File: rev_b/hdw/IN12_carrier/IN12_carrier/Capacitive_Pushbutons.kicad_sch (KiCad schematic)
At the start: 55 parts, among them U905 74LVC1G97, U906 74LVC1G97, U907 74LVC1G97, U908 74LVC1G97, U910 74LVC1G97

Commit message: lots of routing and design progress on IN12 carrier board
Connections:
- net +3V3 renamed +3.3V
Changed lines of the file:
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@@
     )
   )
-  (symbol (lib_id "Analog_Clock-rescue:+3.3V-power") (at 57.15 39.37 0) (unit 1)
+  (symbol (lib_id "power:+3.3V") (at 57.15 39.37 0) (unit 1)
     (in_bom yes) (on_board yes) (dnp no)
     (property "Reference" "#PWR02201" (at 57.15 43.18 0)
@@
     )
   )
-  (symbol (lib_id "Analog_Clock-rescue:+3.3V-power") (at 73.66 140.97 270) (unit 1)
+  (symbol (lib_id "power:+3.3V") (at 73.66 140.97 270) (unit 1)
     (in_bom yes) (on_board yes) (dnp no)
     (property "Reference" "#PWR02209" (at 69.85 140.97 0)
@@
     )
   )
-  (symbol (lib_id "Analog_Clock-rescue:+3.3V-power") (at 57.15 115.57 0) (unit 1)
+  (symbol (lib_id "power:+3.3V") (at 57.15 115.57 0) (unit 1)
     (in_bom yes) (on_board yes) (dnp no)
     (property "Reference" "#PWR02201" (at 57.15 119.38 0)
@@
     )
   )
-  (symbol (lib_id "Analog_Clock-rescue:+3.3V-power") (at 63.5 135.89 0) (unit 1)
+  (symbol (lib_id "power:+3.3V") (at 63.5 135.89 0) (unit 1)
     (in_bom yes) (on_board yes) (dnp no)
     (property "Reference" "#PWR02205" (at 63.5 139.7 0)
@@
     )
   )
-  (symbol (lib_id "Analog_Clock-rescue:+3.3V-power") (at 63.5 97.79 0) (unit 1)
+  (symbol (lib_id "power:+3.3V") (at 63.5 97.79 0) (unit 1)
     (in_bom yes) (on_board yes) (dnp no)
     (property "Reference" "#PWR02205" (at 63.5 101.6 0)
@@
     )
   )
-  (symbol (lib_id "Analog_Clock-rescue:+3.3V-power") (at 63.5 21.59 0) (unit 1)
+  (symbol (lib_id "power:+3.3V") (at 63.5 21.59 0) (unit 1)
     (in_bom yes) (on_board yes) (dnp no)
     (property "Reference" "#PWR02205" (at 63.5 25.4 0)
@@
     )
   )
-  (symbol (lib_id "Analog_Clock-rescue:+3.3V-power") (at 99.06 105.41 0) (unit 1)
+  (symbol (lib_id "power:+3.3V") (at 99.06 105.41 0) (unit 1)
     (in_bom yes) (on_board yes) (dnp no)
     (property "Reference" "#PWR02215" (at 99.06 109.22 0)
@@
     )
   )
-  (symbol (lib_id "Analog_Clock-rescue:+3.3V-power") (at 105.41 39.37 0) (unit 1)
+  (symbol (lib_id "power:+3.3V") (at 105.41 39.37 0) (unit 1)
     (in_bom yes) (on_board yes) (dnp no)
     (property "Reference" "#PWR02219" (at 105.41 43.18 0)
@@
     )
   )
-  (symbol (lib_id "Analog_Clock-rescue:+3.3V-power") (at 73.66 102.87 270) (unit 1)
+  (symbol (lib_id "power:+3.3V") (at 73.66 102.87 270) (unit 1)
     (in_bom yes) (on_board yes) (dnp no)
     (property "Reference" "#PWR02209" (at 69.85 102.87 0)
@@
     )
   )
-  (symbol (lib_id "Analog_Clock-rescue:+3.3V-power") (at 105.41 115.57 0) (unit 1)
+  (symbol (lib_id "power:+3.3V") (at 105.41 115.57 0) (unit 1)
     (in_bom yes) (on_board yes) (dnp no)
     (property "Reference" "#PWR02219" (at 105.41 119.38 0)
@@
     )
   )
-  (symbol (lib_id "Analog_Clock-rescue:+3.3V-power") (at 105.41 77.47 0) (unit 1)
+  (symbol (lib_id "power:+3.3V") (at 105.41 77.47 0) (unit 1)
     (in_bom yes) (on_board yes) (dnp no)
     (property "Reference" "#PWR02219" (at 105.41 81.28 0)
@@
     )
   )
-  (symbol (lib_id "Analog_Clock-rescue:+3.3V-power") (at 63.5 59.69 0) (unit 1)
+  (symbol (lib_id "power:+3.3V") (at 63.5 59.69 0) (unit 1)
     (in_bom yes) (on_board yes) (dnp no)
     (property "Reference" "#PWR02205" (at 63.5 63.5 0)
@@
     )
   )
-  (symbol (lib_id "Analog_Clock-rescue:+3.3V-power") (at 73.66 64.77 270) (unit 1)
+  (symbol (lib_id "power:+3.3V") (at 73.66 64.77 270) (unit 1)
     (in_bom yes) (on_board yes) (dnp no)
     (property "Reference" "#PWR02209" (at 69.85 64.77 0)
@@
     )
   )
-  (symbol (lib_id "Analog_Clock-rescue:+3.3V-power") (at 227.33 29.21 0) (unit 1)
+  (symbol (lib_id "power:+3.3V") (at 227.33 29.21 0) (unit 1)
     (in_bom yes) (on_board yes) (dnp no)
     (property "Reference" "#PWR02215" (at 227.33 33.02 0)
@@
     )
   )
-  (symbol (lib_id "Analog_Clock-rescue:+3.3V-power") (at 99.06 67.31 0) (unit 1)
+  (symbol (lib_id "power:+3.3V") (at 99.06 67.31 0) (unit 1)
     (in_bom yes) (on_board yes) (dnp no)
     (property "Reference" "#PWR02215" (at 99.06 71.12 0)
@@
     )
   )
-  (symbol (lib_id "Analog_Clock-rescue:+3.3V-power") (at 73.66 26.67 270) (unit 1)
+  (symbol (lib_id "power:+3.3V") (at 73.66 26.67 270) (unit 1)
     (in_bom yes) (on_board yes) (dnp no)
     (property "Reference" "#PWR02209" (at 69.85 26.67 0)
@@
     )
   )
-  (symbol (lib_id "Analog_Clock-rescue:+3.3V-power") (at 99.06 143.51 0) (unit 1)
+  (symbol (lib_id "power:+3.3V") (at 99.06 143.51 0) (unit 1)
     (in_bom yes) (on_board yes) (dnp no)
     (property "Reference" "#PWR02215" (at 99.06 147.32 0)
@@
     )
   )
-  (symbol (lib_id "Analog_Clock-rescue:+3.3V-power") (at 57.15 153.67 0) (unit 1)
+  (symbol (lib_id "power:+3.3V") (at 57.15 153.67 0) (unit 1)
     (in_bom yes) (on_board yes) (dnp no)
     (property "Reference" "#PWR02201" (at 57.15 157.48 0)
@@
     )
   )
-  (symbol (lib_id "Analog_Clock-rescue:+3.3V-power") (at 99.06 29.21 0) (unit 1)
+  (symbol (lib_id "power:+3.3V") (at 99.06 29.21 0) (unit 1)
     (in_bom yes) (on_board yes) (dnp no)
     (property "Reference" "#PWR02215" (at 99.06 33.02 0)
@@
     )
   )
-  (symbol (lib_id "Analog_Clock-rescue:+3.3V-power") (at 191.77 21.59 0) (unit 1)
+  (symbol (lib_id "power:+3.3V") (at 191.77 21.59 0) (unit 1)
     (in_bom yes) (on_board yes) (dnp no)
     (property "Reference" "#PWR02205" (at 191.77 25.4 0)
@@
     )
   )
-  (symbol (lib_id "Analog_Clock-rescue:+3.3V-power") (at 233.68 39.37 0) (unit 1)
+  (symbol (lib_id "power:+3.3V") (at 233.68 39.37 0) (unit 1)
     (in_bom yes) (on_board yes) (dnp no)
     (property "Reference" "#PWR02219" (at 233.68 43.18 0)
@@
     )
   )
-  (symbol (lib_id "Analog_Clock-rescue:+3.3V-power") (at 185.42 39.37 0) (unit 1)
+  (symbol (lib_id "power:+3.3V") (at 185.42 39.37 0) (unit 1)
     (in_bom yes) (on_board yes) (dnp no)
     (property "Reference" "#PWR02201" (at 185.42 43.18 0)
@@
     )
   )
-  (symbol (lib_id "Analog_Clock-rescue:+3.3V-power") (at 105.41 153.67 0) (unit 1)
+  (symbol (lib_id "power:+3.3V") (at 105.41 153.67 0) (unit 1)
     (in_bom yes) (on_board yes) (dnp no)
     (property "Reference" "#PWR02219" (at 105.41 157.48 0)
@@
     )
   )
-  (symbol (lib_id "Analog_Clock-rescue:+3.3V-power") (at 201.93 26.67 270) (unit 1)
+  (symbol (lib_id "power:+3.3V") (at 201.93 26.67 270) (unit 1)
     (in_bom yes) (on_board yes) (dnp no)
     (property "Reference" "#PWR02209" (at 198.12 26.67 0)
@@
     )
   )
-  (symbol (lib_id "Analog_Clock-rescue:+3.3V-power") (at 57.15 77.47 0) (unit 1)
+  (symbol (lib_id "power:+3.3V") (at 57.15 77.47 0) (unit 1)
     (in_bom yes) (on_board yes) (dnp no)
     (property "Reference" "#PWR02201" (at 57.15 81.28 0)

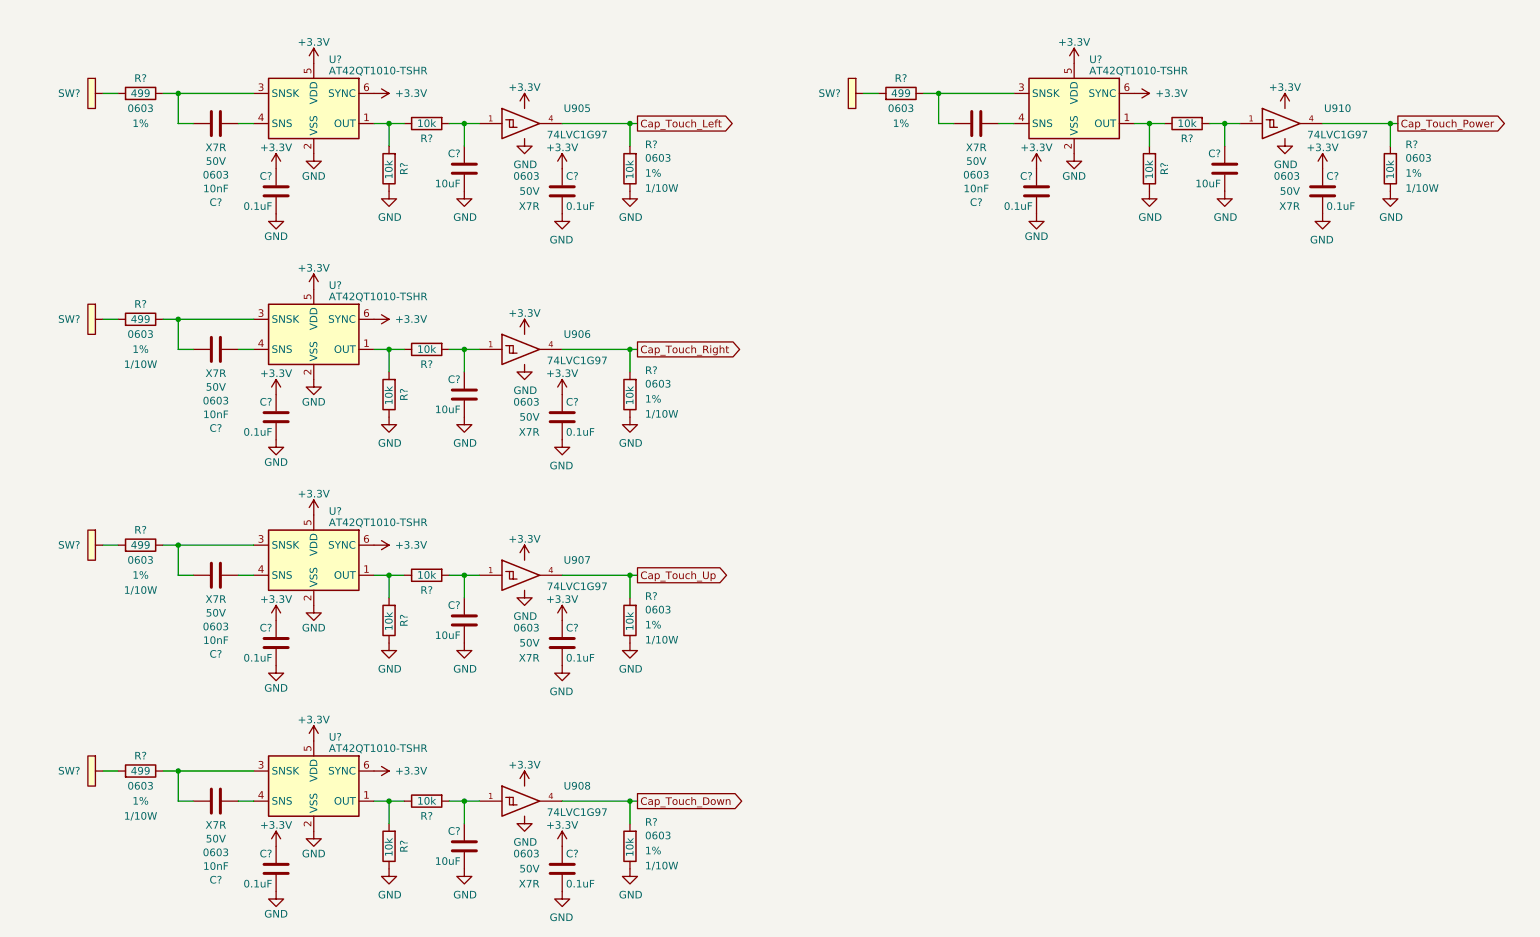
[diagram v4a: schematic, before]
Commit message: added cap touch sensors back
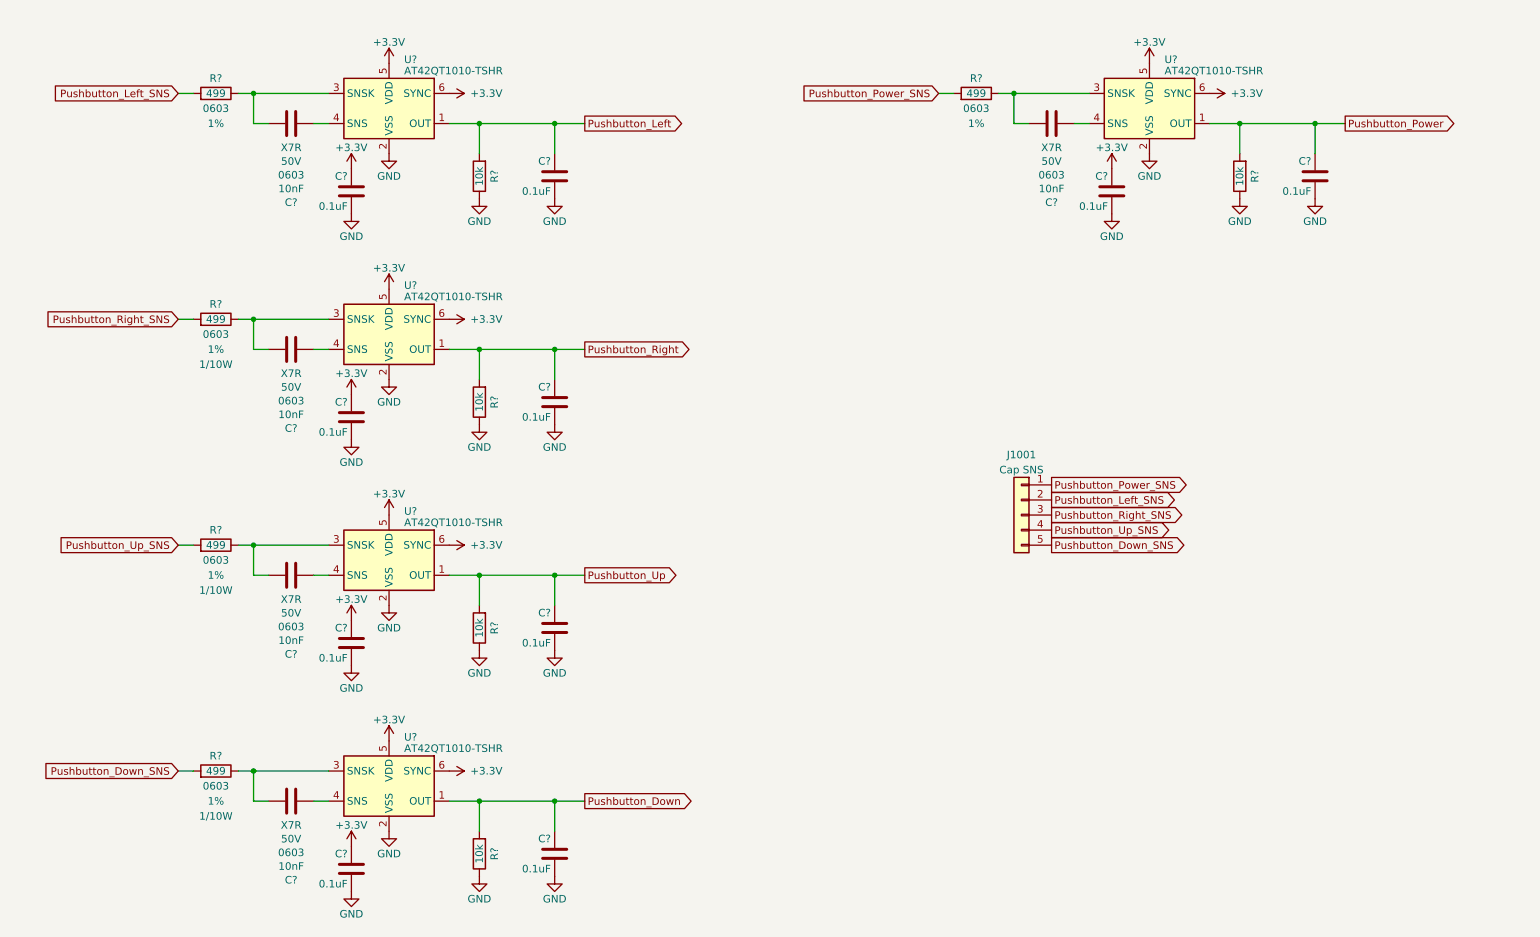
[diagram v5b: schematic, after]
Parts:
- removed C? (x5): 0.1uF, Capacitors_SMD:C_0603, symbol Custom_Library:C_Custom
- removed C? (x5): 10uF, Capacitors_SMD:C_0603, symbol Custom_Library:C_Custom
- removed R? (x15): 10k, Resistors_SMD:R_0603, symbol Custom_Library:R_Custom
- removed SW? (x5): Cap_Touch, Custom Footprints Library:Capacitive_Touch_Pad, symbol Custom_Library:Cap_Touch
- removed U905, U906, U907, U908, U910: 74LVC1G97, Package_TO_SOT_SMD:SOT-363_SC-70-6, symbol Custom Library:74LVC1G97_Power_BUF
- added C? (x5): 0.1uF, Capacitors_SMD:C_0603, symbol Custom_Library:C_Custom
- added J1001: Cap SNS, Connector_PinHeader_2.54mm:PinHeader_1x05_P2.54mm_Horizontal, symbol Connector_Generic:Conn_01x05
- added R? (x5): 10k, Resistors_SMD:R_0603, symbol Custom_Library:R_Custom
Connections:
- net GND: now also C?.2, C?.2, C?.2, C?.2, C?.2, R?.2, R?.2, R?.2, R?.2, R?.2
- net Pushbutton_Right: now reaches U?.1 (OUT)
- net Pushbutton_Right: now also C?.1, R?.1
- net Pushbutton_Up_SNS: now reaches R?.1
- net Pushbutton_Up_SNS: now also J1001.4 (Pin_4)
- net Pushbutton_Right_SNS: now reaches R?.1
- net Pushbutton_Right_SNS: now also J1001.3 (Pin_3)
- net Pushbutton_Up: now reaches U?.1 (OUT)
- net Pushbutton_Up: now also C?.1, R?.1
- net Pushbutton_Power: now reaches U?.1 (OUT)
- net Pushbutton_Power: now also C?.1, R?.1
- net Pushbutton_Left_SNS: now reaches R?.1
- net Pushbutton_Left_SNS: now also J1001.2 (Pin_2)
- net Pushbutton_Power_SNS: now reaches R?.1
- net Pushbutton_Power_SNS: now also J1001.1 (Pin_1)
- net Pushbutton_Down: now reaches U?.1 (OUT)
- net Pushbutton_Down: now also C?.1, R?.1
- net Pushbutton_Down_SNS: now reaches R?.1
- net Pushbutton_Down_SNS: now also J1001.5 (Pin_5)
- net Pushbutton_Left: now reaches U?.1 (OUT)
- net Pushbutton_Left: now also C?.1, R?.1
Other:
- moved on the sheet: C?, R?, U?
